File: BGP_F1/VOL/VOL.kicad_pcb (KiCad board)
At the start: 4 copper layers, 40 x 30 mm, 26 parts, among them P1 CONN_01X05, P2 CONN_01X05, P3 CONN_01X05, P4 CONN_01X03, P5 CONN_01X02, P6 CONN_02X02, P7 CONN_01X12, U1 MC33178, U2 MC33178

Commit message: f1 pcb complete
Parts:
- C3, R12, R13: moved to B.Cu
- moved R4 14.1 mm to (168.8, 80.0)
- moved C2 10.8 mm to (154.0, 83.7)
- moved R9 10.2 mm to (147.0, 83.7), turned to 180 degrees
- moved R10 8.56 mm to (156.0, 87.5)
- moved R5 8.56 mm to (152.0, 96.1), turned to 270 degrees
- moved C3 6.57 mm to (140.4, 85.9), turned to 180 degrees
- moved R13 6.36 mm to (140.4, 83.2), turned to 0 degrees
- moved R12 5.97 mm to (136.4, 84.6)
- moved R6 4.97 mm to (152.0, 78.7)
- moved R7 4.88 mm to (152.0, 81.1)
- moved C4 4.60 mm to (160.4, 96.4), turned to 180 degrees
- moved U1 4.04 mm to (139.0, 88.0)
- moved U2 4.04 mm to (139.1, 80.8)
- moved C1 2.92 mm to (147.0, 78.7)
- moved R11 2.91 mm to (160.6, 92.8), turned to 0 degrees
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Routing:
- net Earth: track 9.49 -> 81.5 mm, vias 5 -> 2
- net /V+: track 3.98 -> 59.9 mm, vias 3 -> 0
- net Net-(C1-Pad2): track 17.6 -> 33.5 mm, vias 0 -> 2
- net /PB1_1: track 36.1 -> 48.8 mm
- net /Vref: track 7.52 -> 19.5 mm, vias 4 -> 2
- net /PB2_3: track 25.9 -> 37.7 mm, vias 1 -> 2
- net /OUT_HPF: track 12.0 -> 3.75 mm
- net Net-(C1-Pad1): track 19.1 -> 11.2 mm
- net /OUT_N: track 18.9 -> 24.9 mm
- net /OUT: track 18.5 -> 24.1 mm
- net /PB2_2: track 13.4 -> 18.9 mm
- net Net-(C3-Pad1): track 8.00 -> 12.6 mm, vias 0 -> 1
- net /OUT_B: track 17.6 -> 19.9 mm, vias 0 -> 1
- net /PB1_2: track 15.1 -> 13.2 mm
- net /PV_3: track 9.07 -> 8.08 mm
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- added copper zone on F.Cu, net (none)
- added copper zone on B.Cu, net /Vref
- removed copper zone on B.Cu, net /V+
- removed copper zone on In2.Cu, net /Vref
- removed copper zone on In1.Cu, net Earth
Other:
- copper layers 4 -> 2

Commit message: F1 pcb trimmed
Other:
- board size 40 x 30 mm -> 38 x 30 mm
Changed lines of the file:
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@@
     (links 63)
     (no_connects 0)
-    (area 129.924999 75.924999 170.075001 106.075001)
+    (area 129.924999 75.524999 171.65588 107.305)
     (thickness 1.6)
     (drawings 8)
@@
   )
   (gr_line (start 169.7 105.7) (end 169.7 76.3) (layer Margin) (width 0.2))
-  (gr_line (start 130.3 105.7) (end 169.7 105.7) (layer Margin) (width 0.2))
-  (gr_line (start 130.3 76.3) (end 130.3 105.7) (layer Margin) (width 0.2))
-  (gr_line (start 169.7 76.3) (end 130.3 76.3) (layer Margin) (width 0.2))
+  (gr_line (start 132.3 105.7) (end 169.7 105.7) (layer Margin) (width 0.2))
+  (gr_line (start 132.3 76.3) (end 132.3 105.7) (layer Margin) (width 0.2))
+  (gr_line (start 169.7 76.3) (end 132.3 76.3) (layer Margin) (width 0.2))
   (gr_line (start 170 76) (end 170 106) (layer Edge.Cuts) (width 0.15))
-  (gr_line (start 130 106) (end 170 106) (layer Edge.Cuts) (width 0.15))
-  (gr_line (start 130 76) (end 130 106) (layer Edge.Cuts) (width 0.15))
-  (gr_line (start 170 76) (end 130 76) (layer Edge.Cuts) (width 0.15))
+  (gr_line (start 132 106) (end 170 106) (layer Edge.Cuts) (width 0.15))
+  (gr_line (start 132 76) (end 132 106) (layer Edge.Cuts) (width 0.15))
+  (gr_line (start 170 76) (end 132 76) (layer Edge.Cuts) (width 0.15))
   (segment (start 148.1 81.1) (end 148.1 82.0003) (width 0.3) (layer F.Cu) (net 1))
   (segment (start 146.9503 83.15) (end 148.1 82.0003) (width 0.3) (layer F.Cu) (net 1))
@@
     (polygon
       (pts
-        (xy 169.7 76.3) (xy 130.3 76.3) (xy 130.3 105.7) (xy 169.7 105.7)
+        (xy 169.7 76.3) (xy 132.3 76.3) (xy 132.3 105.7) (xy 169.7 105.7)
       )
     )
@@
     (polygon
       (pts
-        (xy 169.7 76.3) (xy 130.3 76.3) (xy 130.3 105.7) (xy 169.7 105.7)
+        (xy 169.7 76.3) (xy 132.2 76.2) (xy 132.2 105.6) (xy 169.7 105.7)
       )
     )

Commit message: F1 VOL Prot Diode
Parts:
- added D1: 1N4148, Diodes_SMD:D_SOD-123, B.Cu at (160.8, 102.2)
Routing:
- net Earth: track 81.5 -> 52.8 mm, vias 2 -> 3
- net /V+: track 59.9 -> 65.5 mm
- net /PB1_1: track 48.8 -> 45.9 mm
- net Net-(C1-Pad2): track 33.5 -> 35.0 mm
- net /OUT: track 24.1 -> 24.8 mm
- net /PB1_2: track 13.2 -> 12.6 mm
- added copper zone on F.Cu, net Earth
- removed copper zone on F.Cu, net (none)

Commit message: F boards routed, various optimisations made
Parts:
- D1: footprint Diodes_SMD:D_SOD-123 -> Diodes_SMD:DO-214BA; moved to F.Cu
- moved D1 0.22 mm to (160.7, 102.0)
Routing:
- net Earth: track 52.8 -> 40.8 mm
- net /V+: track 65.5 -> 70.7 mm
- net /OUT: track 24.8 -> 29.0 mm

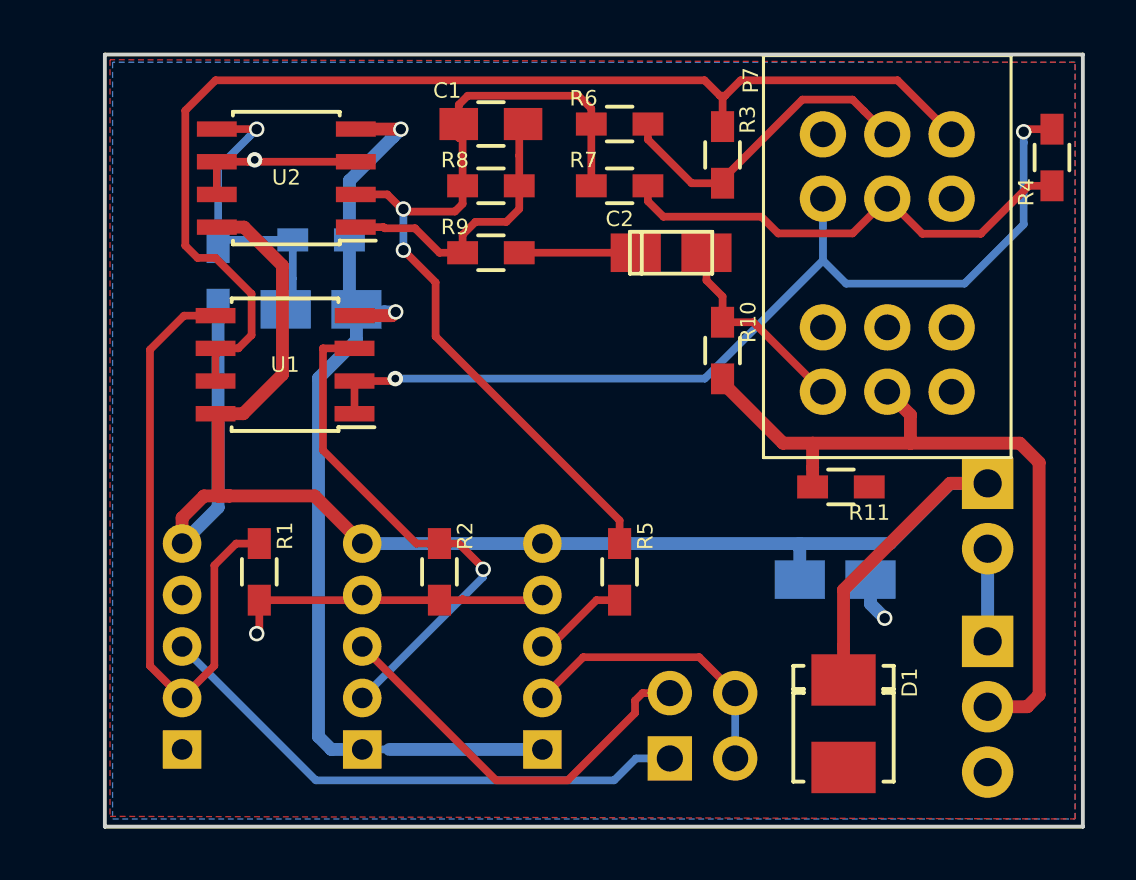
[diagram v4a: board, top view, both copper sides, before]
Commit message: Hand route F VOL board
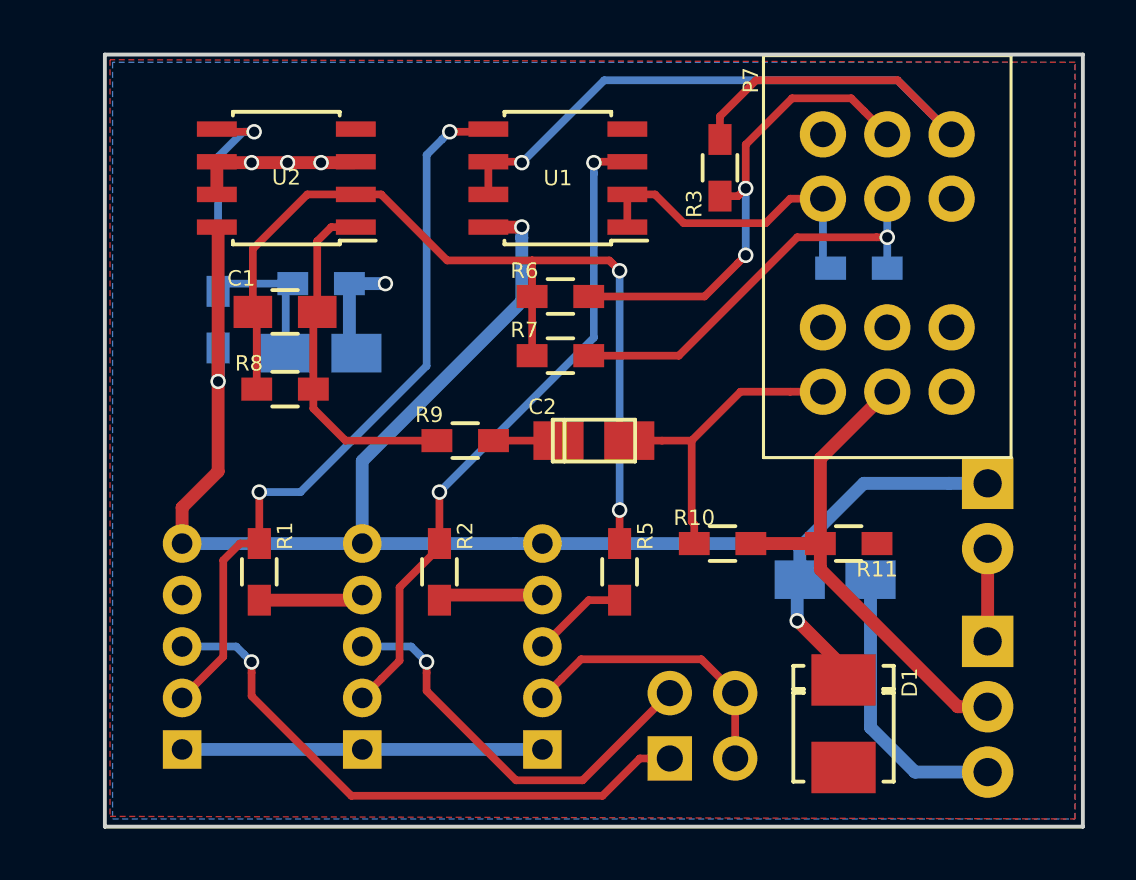
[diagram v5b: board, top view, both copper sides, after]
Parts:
- R4: moved to B.Cu
- moved U1 12.8 mm to (149.6, 80.8)
- moved R8 11.2 mm to (139.0, 89.0)
- moved C1 10.8 mm to (139.0, 86.0)
- moved R4 8.65 mm to (161.3, 84.3), turned to 180 degrees
- moved C2 7.89 mm to (151.0, 91.0)
- moved R10 7.50 mm to (156.0, 95.0), turned to 0 degrees
- moved R9 7.37 mm to (146.0, 91.0)
- moved R6 7.08 mm to (149.7, 85.4)
- moved R7 6.99 mm to (149.7, 87.7)
- moved R11 2.22 mm to (160.9, 95.0)
- moved R12 1.70 mm to (136.4, 86.3)
- moved R13 1.70 mm to (140.4, 84.9)
- moved C3 1.70 mm to (140.4, 87.6)
- moved R3 0.51 mm to (155.9, 80.4)
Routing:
- net /PB2_3: track 37.7 -> 12.5 mm, vias 2 -> 0
- net /PB1_1: track 45.9 -> 32.8 mm, vias 0 -> 1
- net Earth: track 40.8 -> 30.4 mm, vias 3 -> 1
- net /OUT: track 29.0 -> 19.4 mm
- net /PB1_2: track 12.6 -> 19.0 mm, vias 0 -> 2
- net /OUT_B: track 20.3 -> 25.8 mm, vias 1 -> 2
- net /Vref: track 19.4 -> 14.9 mm, vias 2 -> 3
- net /PV_3: track 7.98 -> 12.4 mm
- net /OUT_N: track 24.9 -> 29.2 mm, vias 0 -> 2
- net /PB2_2: track 18.7 -> 16.2 mm, vias 0 -> 1
- net Net-(C1-Pad1): track 11.2 -> 13.6 mm
- net /V+: track 70.7 -> 68.7 mm, vias 0 -> 3
- net Net-(C2-Pad1): track 4.53 -> 2.53 mm
- net Net-(C3-Pad1): track 12.6 -> 14.5 mm
- net Net-(C1-Pad2): track 35.0 -> 36.3 mm
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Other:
- net class PWR added: clearance 0.3, trace_width 0.5, via_dia 0.6, via_drill 0.4

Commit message: F VOL
POT EARTH FIXUP
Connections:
- P7 pad 10: /Vref -> Earth
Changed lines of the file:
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@@
-(kicad_pcb (version 4) (host pcbnew 4.0.4-1.fc24-product)
+(kicad_pcb (version 4) (host pcbnew 4.0.7)
   (general
     (links 65)
     (no_connects 0)
-    (area 131.924999 75.524999 171.65588 107.305)
+    (area 131.924999 75.924999 170.075001 106.075001)
     (thickness 1.6)
     (drawings 8)
@@
       (net 13 /OUT))
     (pad 10 thru_hole circle (at -10 0 90) (size 1.8 1.8) (drill 1) (layers *.Cu *.Mask)
-      (net 21 /Vref))
+      (net 6 Earth))
     (pad 1 thru_hole circle (at 0 0 90) (size 1.8 1.8) (drill 1) (layers *.Cu *.Mask)
       (net 14 /PB1_1))
@@
   (segment (start 147.1 91) (end 149.62586 91) (width 0.3) (layer F.Cu) (net 3))
   (segment (start 154.9 95) (end 154.9 94.25) (width 0.3) (layer F.Cu) (net 4))
+  (segment (start 154.8 94.15) (end 154.8 91) (width 0.3) (layer F.Cu) (net 4))
   (segment (start 154.9 94.25) (end 154.8 94.15) (width 0.3) (layer F.Cu) (net 4))
-  (segment (start 154.8 94.15) (end 154.8 91) (width 0.3) (layer F.Cu) (net 4))
   (segment (start 154.8 91) (end 156.7 89.1) (width 0.3) (layer F.Cu) (net 4))
   (segment (start 156.7 89.1) (end 158.627208 89.1) (width 0.3) (layer F.Cu) (net 4))
@@
   (segment (start 135 99) (end 137.1 99) (width 0.3) (layer B.Cu) (net 8))
   (via (at 137.7 99.6) (size 0.6) (drill 0.4) (layers F.Cu B.Cu) (net 8))
+  (segment (start 158.99986 95.14943) (end 161.48929 92.66) (width 0.5) (layer B.Cu) (net 9))
+  (segment (start 164.80051 92.66) (end 166.3 92.66) (width 0.5) (layer B.Cu) (net 9))
+  (segment (start 161.48929 92.66) (end 164.80051 92.66) (width 0.5) (layer B.Cu) (net 9))
   (segment (start 148.195 82.705) (end 148.2 82.7) (width 0.5) (layer F.Cu) (net 9))
   (segment (start 146.9 82.705) (end 148.195 82.705) (width 0.5) (layer F.Cu) (net 9))
@@
   (segment (start 160.7 99.8) (end 158.9 98) (width 0.5) (layer F.Cu) (net 9))
   (via (at 158.9 98) (size 0.6) (drill 0.4) (layers F.Cu B.Cu) (net 9))
-  (segment (start 158.99986 95.14943) (end 161.48929 92.66) (width 0.5) (layer B.Cu) (net 9))
-  (segment (start 161.48929 92.66) (end 164.80051 92.66) (width 0.5) (layer B.Cu) (net 9))
-  (segment (start 164.80051 92.66) (end 166.3 92.66) (width 0.5) (layer B.Cu) (net 9))
   (segment (start 151 87) (end 151 80.624264) (width 0.3) (layer B.Cu) (net 10))
   (segment (start 145 93) (end 151 87) (width 0.3) (layer B.Cu) (net 10))
@@
   (via (at 144.500002 99.6) (size 0.6) (drill 0.4) (layers F.Cu B.Cu) (net 11))
   (segment (start 166.3 95.2) (end 166.3 98.8) (width 0.5) (layer F.Cu) (net 12))
-  (segment (start 166.3 101.34) (end 165.14 101.34) (width 0.5) (layer F.Cu) (net 13))
-  (segment (start 159.8 96) (end 159.8 95.95) (width 0.5) (layer F.Cu) (net 13))
-  (segment (start 165.14 101.34) (end 159.8 96) (width 0.5) (layer F.Cu) (net 13))
-  (segment (start 159.8 95.95) (end 159.8 95) (width 0.5) (layer F.Cu) (net 13))
-  (segment (start 159.8 95) (end 157.1 95) (width 0.5) (layer F.Cu) (net 13))
   (segment (start 159.8 95) (end 159.8 91.7) (width 0.5) (layer F.Cu) (net 13))
   (segment (start 159.8 91.7) (end 162.4 89.1) (width 0.5) (layer F.Cu) (net 13))
+  (segment (start 166.3 101.34) (end 165.14 101.34) (width 0.5) (layer F.Cu) (net 13))
+  (segment (start 159.8 95.95) (end 159.8 95) (width 0.5) (layer F.Cu) (net 13))
+  (segment (start 165.14 101.34) (end 159.8 96) (width 0.5) (layer F.Cu) (net 13))
+  (segment (start 159.8 96) (end 159.8 95.95) (width 0.5) (layer F.Cu) (net 13))
+  (segment (start 159.8 95) (end 157.1 95) (width 0.5) (layer F.Cu) (net 13))
   (segment (start 148.2 80.2) (end 151.4 77) (width 0.3) (layer B.Cu) (net 14))
   (segment (start 151.4 77) (end 162.8 77) (width 0.3) (layer B.Cu) (net 14))

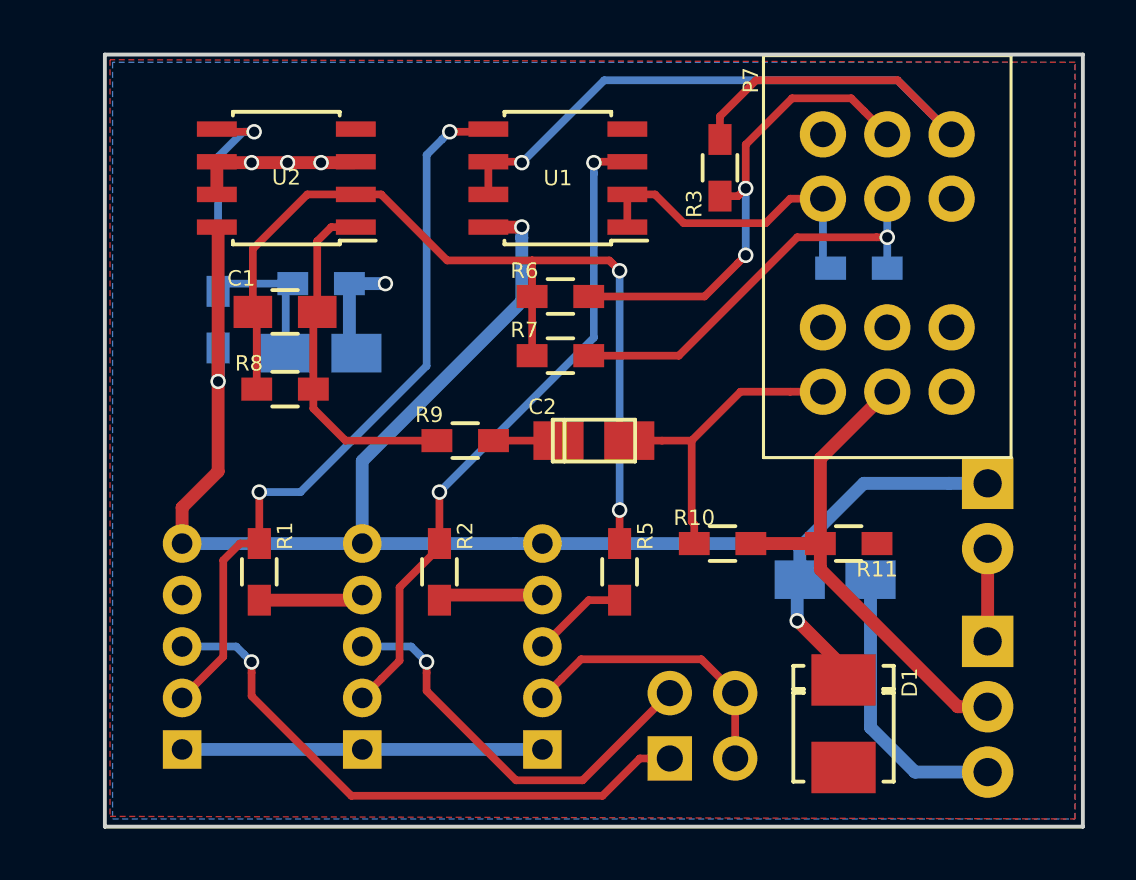
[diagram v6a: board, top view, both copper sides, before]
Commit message: Flipped boards so that they should be facing the right way
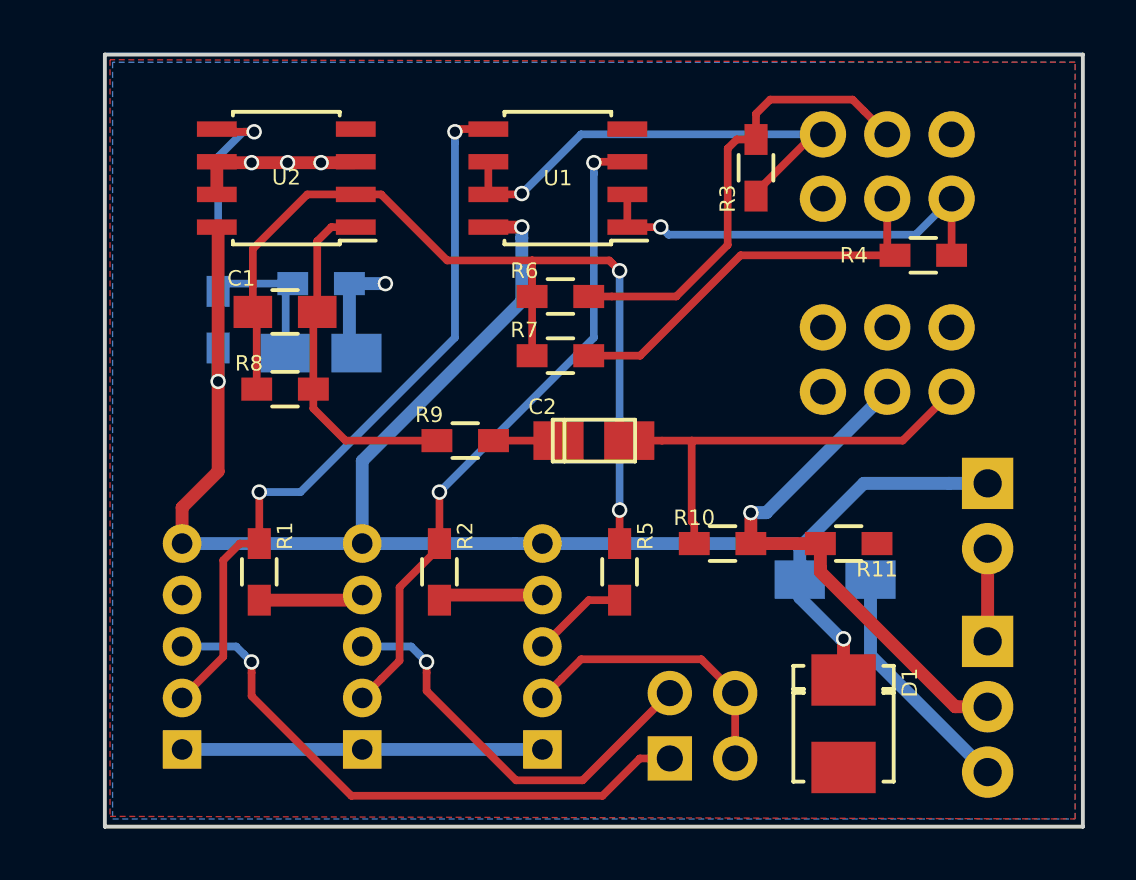
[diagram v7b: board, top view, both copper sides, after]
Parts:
- P7: moved to B.Cu
- R4: moved to F.Cu
- moved P7 5.00 mm to (159.9, 79.1)
- moved R4 2.55 mm to (163.8, 83.8), turned to 0 degrees
- moved R3 1.40 mm to (157.3, 80.4), turned to 270 degrees
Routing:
- net /PB1_1: track 32.8 -> 19.0 mm
- net /PV_3: track 12.4 -> 17.4 mm
- net /PB2_3: track 12.5 -> 16.8 mm, vias 0 -> 1
- net Earth: track 30.4 -> 28.8 mm
- net /OUT: track 19.4 -> 20.9 mm, vias 0 -> 1
- net /V+: track 68.7 -> 69.5 mm
- net /PB1_2: track 19.0 -> 18.3 mm, vias 2 -> 0
- net /PB2_2: track 16.2 -> 15.8 mm, vias 1 -> 0

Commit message: Updated F_VOL
Using 10kB, 100kA pot with correct orientation, and pot correction for blend.
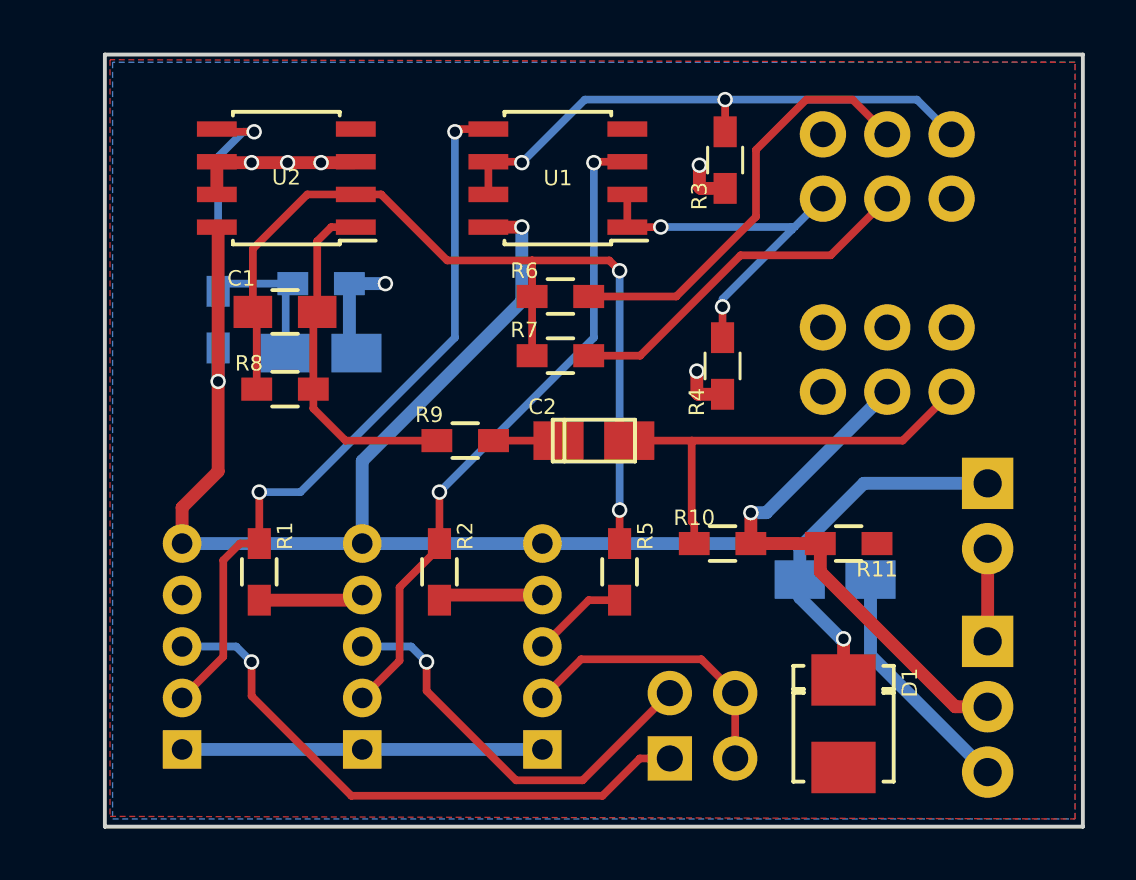
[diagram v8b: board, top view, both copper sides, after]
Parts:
- R3, R4: value 4.99k -> 11.1k
- moved R4 8.91 mm to (156.0, 88.1), turned to 90 degrees
- moved R3 1.24 mm to (156.1, 80.1), turned to 90 degrees
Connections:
- P7 pad 1: /PB1_1 -> /Vref
- P7 pad 3: /Vref -> /PB1_1
- P7 pad 4: /Vref -> /PB2_1
- P7 pad 6: /PB2_3 -> /Vref
- R3 pad 1: /PB1_2 -> /Vref
- R4 pad 1: /PB2_2 -> /Vref
- R4 pad 2: /PB2_3 -> /PB2_1
- U1 pad 1: /PB2_3 -> /PB2_1
- U1 pad 2: /PB2_3 -> /PB2_1
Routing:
- net /PB2_3: track 16.8 -> 0.00 mm, vias 1 -> 0
- net /PB2_1: track 0.00 -> 14.7 mm, vias 0 -> 2
- net /Vref: track 14.9 -> 18.6 mm, vias 3 -> 5
- net /PB1_1: track 19.0 -> 22.2 mm, vias 1 -> 2
- net /PB2_2: track 15.8 -> 14.1 mm
- net /PB1_2: track 18.3 -> 16.8 mm
